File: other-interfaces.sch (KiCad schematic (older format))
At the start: 24 parts, among them J5 DM3AT-SF-PEJM5, J7 BM04B-SRSS-TB-LF-SN, U23 NTS0102GT

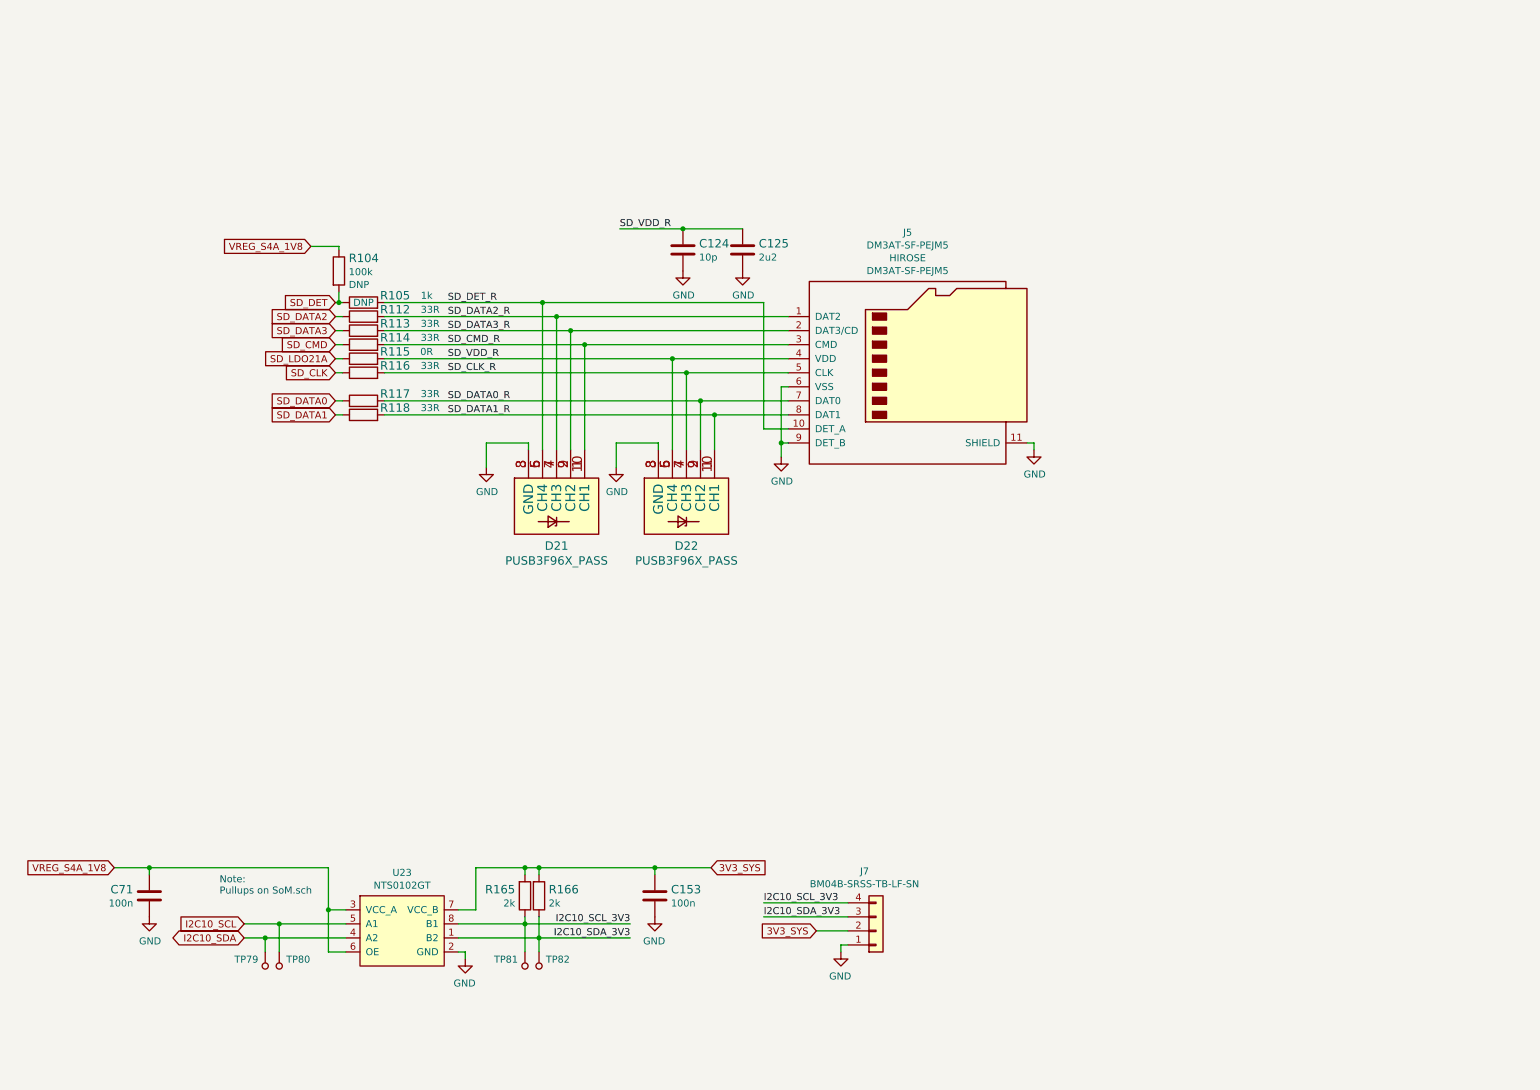
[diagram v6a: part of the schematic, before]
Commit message: Reorganize schematics, add descriptions in top left corner
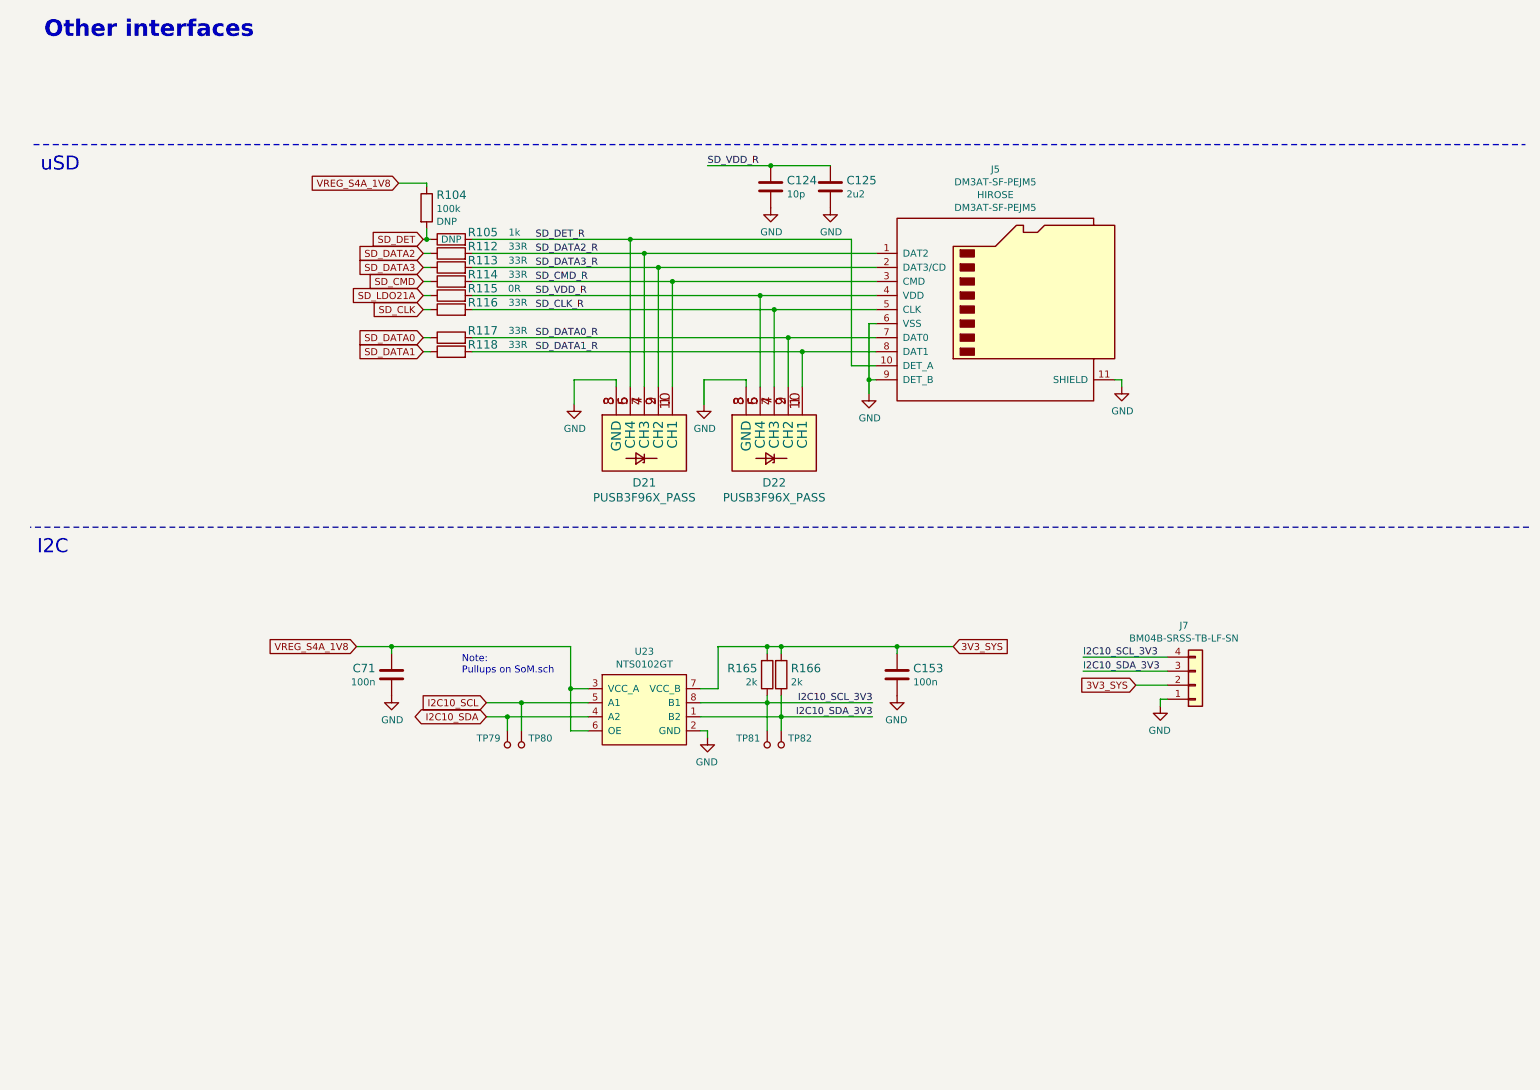
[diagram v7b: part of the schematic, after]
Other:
- note added: "I2C"
- note added: "Other interfaces"
- note added: "uSD"
- moved on the sheet: C124, C125, C153, C71, D21, D22, J5, J7, R104, R105, R112, R113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

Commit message: Clear annotation and annotate
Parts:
- renumbered C71 to C117, C124 to C118, C125 to C119, C153 to C120, D21 to D22, D22 to D23, J5 to J8, J7 to J9, R116 to R100, R117 to R101, R118 to R102, R165 to R103, R166 to R104, R104 to R94, R105 to R95, R112 to R96, R113 to R97, R114 to R98, R115 to R99, TP79 to TP44, TP80 to TP45, TP81 to TP46, TP82 to TP47, U23 to U16
